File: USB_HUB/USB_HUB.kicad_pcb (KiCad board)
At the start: 2 copper layers, 100 x 30 mm, 24 parts, among them J1 USB_C_Receptacle_USB2.0_16P, J2 USB_A, J3 USB_A, J4 USB_A, J5 USB_A, U1 SL2.1A

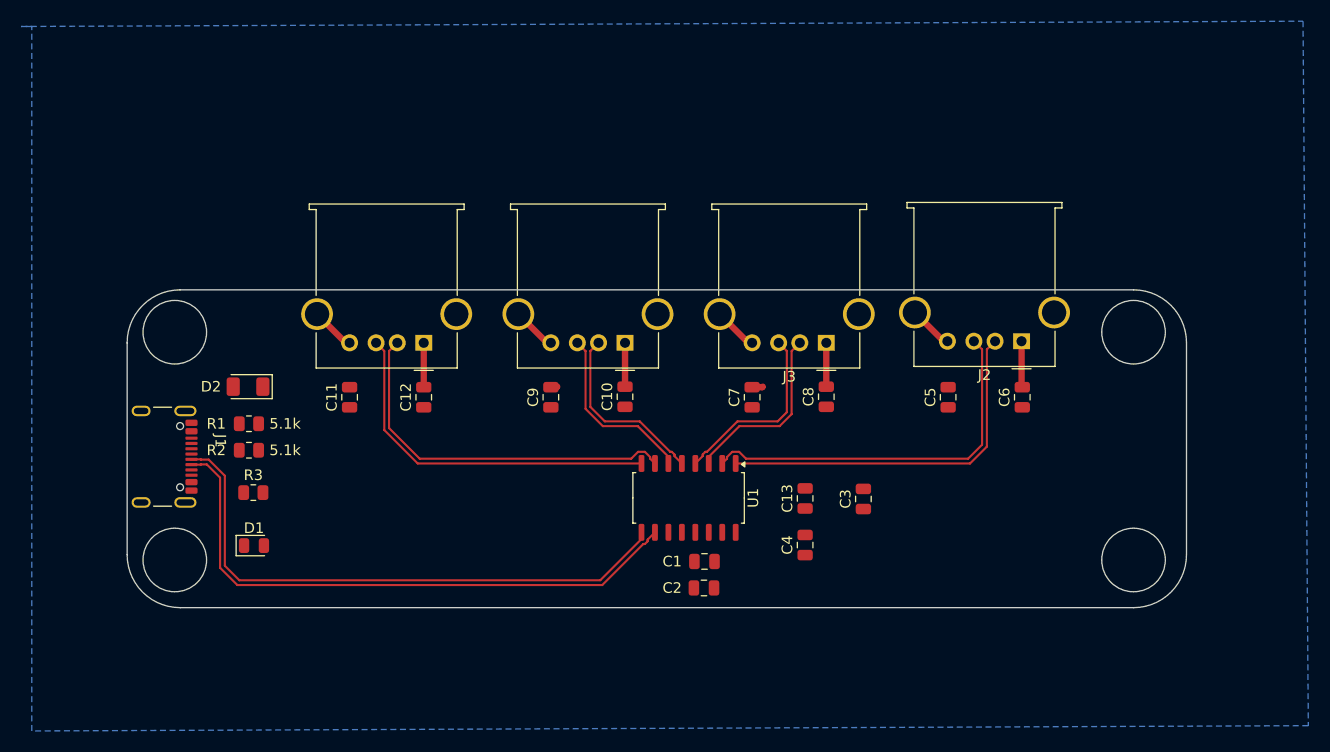
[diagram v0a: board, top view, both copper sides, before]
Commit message: vbus和铺铜
vbus和铺铜结束了，差分电路阻抗没调，fuse不是poly的
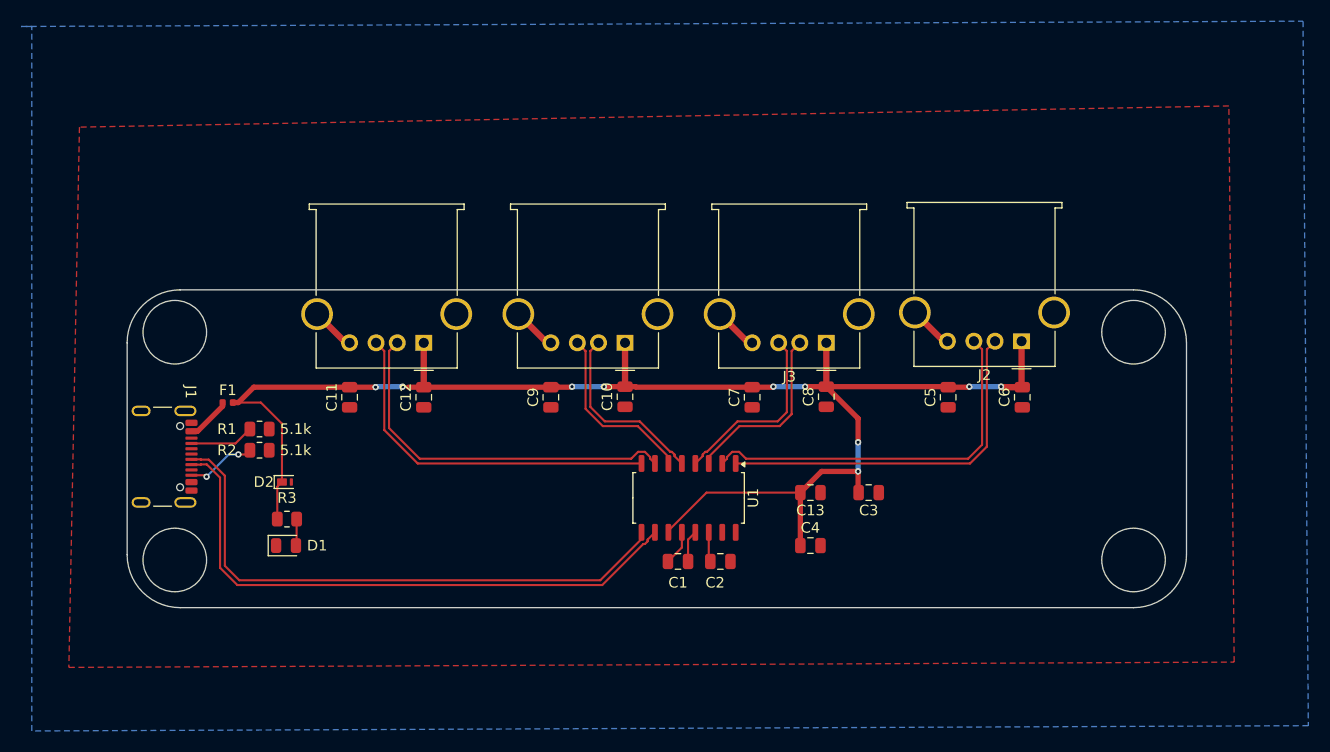
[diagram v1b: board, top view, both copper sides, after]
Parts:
- added F1: Fuse, Fuse:Fuse_0402_1005Metric, F.Cu at (99.5, 98.5)
- C11: value 1uF -> 10uF
- D2: value sd1206t020s1r0 -> PTVS5V0Z1USK; footprint Diode_SMD:D_1206_3216Metric -> Diode_SMD:Nexperia_DSN1608-2_1.6x0.8mm
- moved D2 9.65 mm to (104.9, 106.0), turned to 0 degrees
- moved R3 4.04 mm to (105.1, 109.5)
- moved D1 3.03 mm to (105.0, 112.0)
- moved C2 2.94 mm to (146.0, 113.5)
- moved C1 2.50 mm to (142.0, 113.5)
- moved R1 1.12 mm to (102.5, 101.0)
- moved R2 1.00 mm to (102.5, 103.0)
- moved C3 0.78 mm to (160.0, 107.0), turned to 180 degrees
- moved C13 0.74 mm to (154.5, 107.0), turned to 180 degrees
- moved C4 0.50 mm to (154.5, 112.0), turned to 0 degrees
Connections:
- D2 pad 2: Net-(D2-A) -> GND
- J1 pad A4: Net-(D2-A) -> Net-(F1-Pad1)
- J1 pad A9: Net-(D2-A) -> Net-(F1-Pad1)
- J1 pad B4: Net-(D2-A) -> Net-(F1-Pad1)
- J1 pad B9: Net-(D2-A) -> Net-(F1-Pad1)
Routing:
- net /VBUS: track 18.6 -> 144.1 mm, vias 0 -> 10
- net Net-(J1-CC2): track 0.00 -> 6.61 mm, vias 0 -> 2
- net Net-(J1-CC1): track 0.00 -> 6.08 mm
- net Net-(F1-Pad1): track 0.00 -> 4.26 mm
- net GND: track 16.8 -> 20.1 mm
- net Net-(U1-VDD3): track 0.00 -> 3.03 mm
- net Net-(U1-VDD18): track 0.00 -> 2.81 mm
- net Net-(D1-A): track 0.00 -> 2.53 mm
- added copper zone on F.Cu, net GND
